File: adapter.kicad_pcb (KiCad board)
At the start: 2 copper layers, 15 parts, among them P1 CONN_02X05, P3 CONN_02X06, Q1 BSS138, U1 MC34063

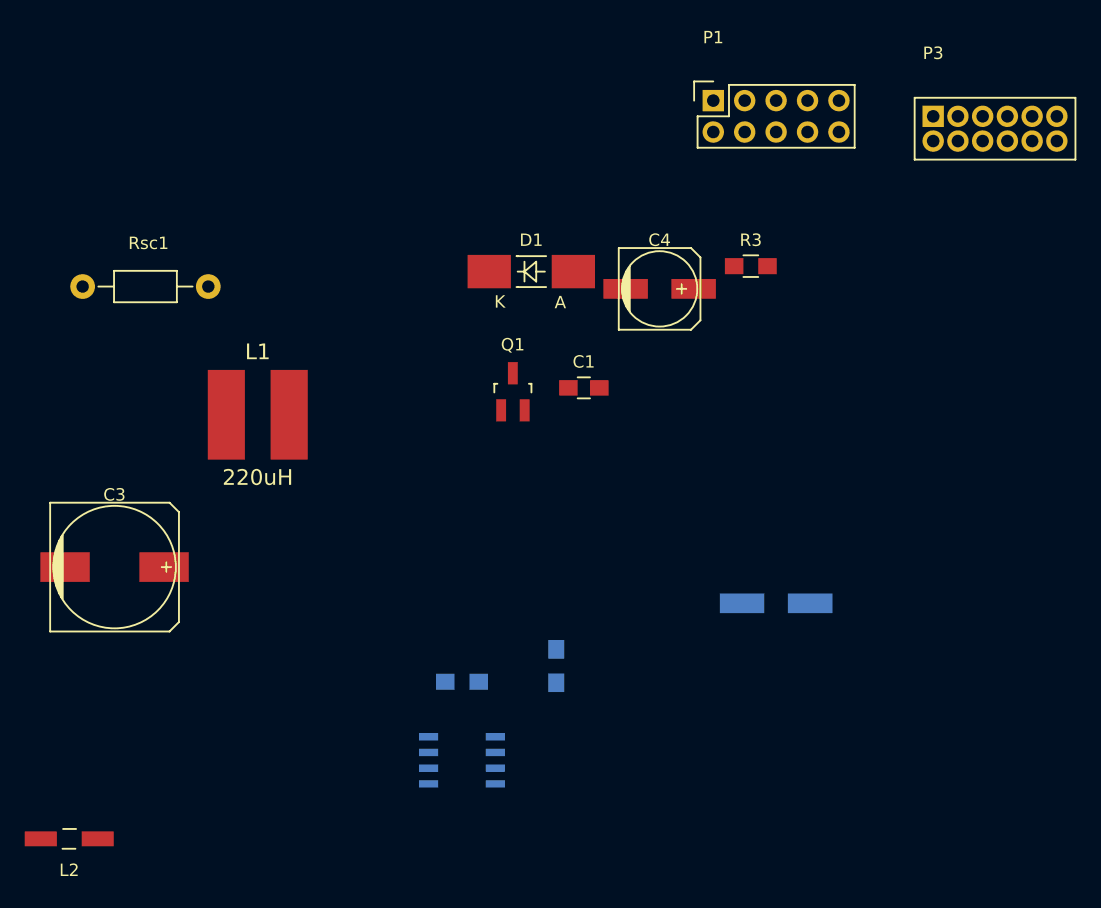
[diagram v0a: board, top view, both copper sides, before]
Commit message: Changed 2mm pitch array footpring a little.
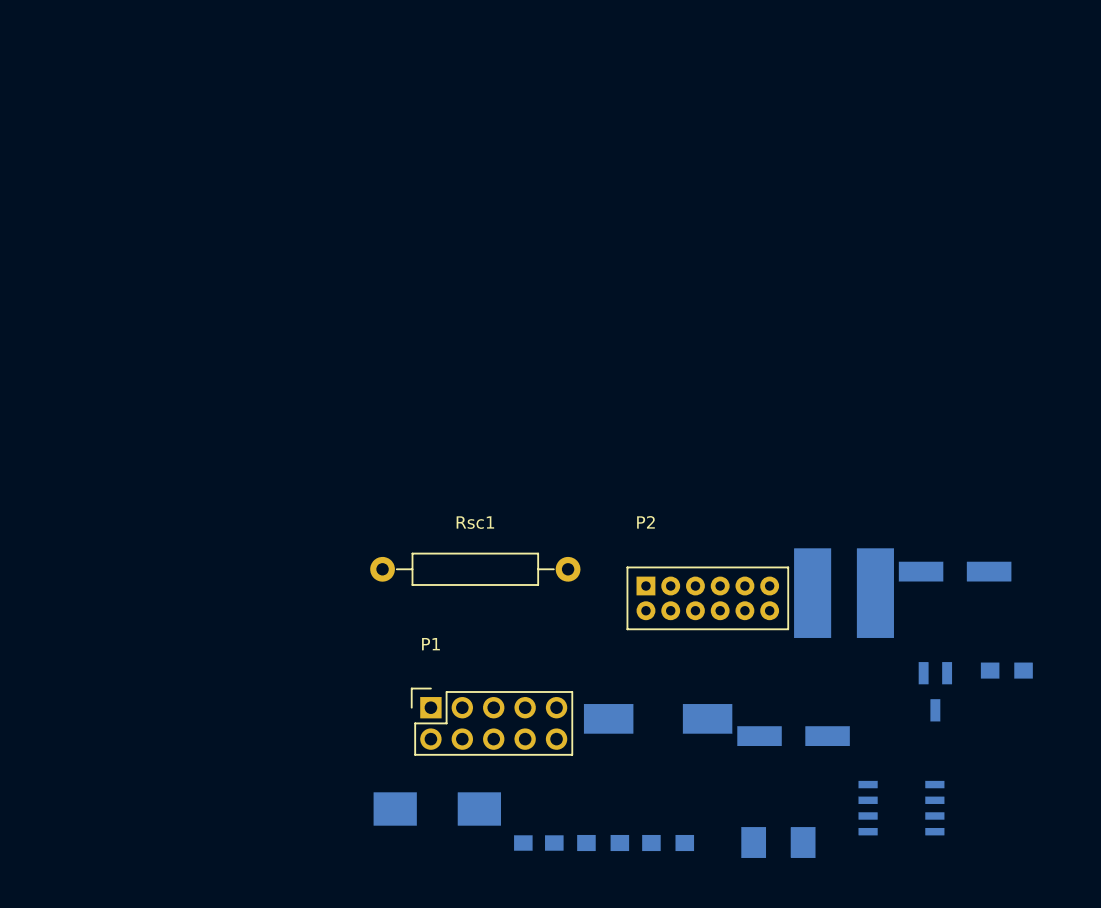
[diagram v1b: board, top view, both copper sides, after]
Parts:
- removed P3: CONN_02X06, DSMX Tx module adapter:Socket_Strip_Straight_2x06_pitch2mm
- added P2: CONN_02X06, DSMX Tx module adapter:Socket_Strip_Straight_2x06_pitch2mm, F.Cu at (181.2, 101.5)
- C1, C3, D1, L1, Q1, R3: moved to B.Cu
- C4: footprint Capacitors_SMD:c_elec_6.3x5.7 -> Capacitors_SMD:c_elec_6.3x7.7; moved to B.Cu
- L2: footprint Choke_SMD:Choke_SMD_1206_Handsoldering -> Capacitors_SMD:C_1210_HandSoldering; moved to B.Cu
- Rsc1: footprint Resistors_ThroughHole:Resistor_Horizontal_RM10mm -> Resistors_ThroughHole:Resistor_Horizontal_RM15mm
- moved L2 57.3 mm to (192.0, 122.2), turned to 0 degrees
- moved P1 54.1 mm to (163.9, 111.3)
- moved L1 49.5 mm to (197.3, 102.1)
- moved C3 45.6 mm to (182.2, 112.2)
- moved D1 44.1 mm to (164.4, 119.5)
- moved Q1 41.9 mm to (204.6, 110.0)
- moved R3 38.7 mm to (210.4, 108.3)
- moved C1 37.0 mm to (172.6, 122.3)
- moved U1 35.7 mm to (201.9, 119.4)
- moved Rsc1 35.1 mm to (167.4, 100.1)
- moved C4 33.1 mm to (206.2, 100.3)
- moved R1 17.3 mm to (177.8, 122.3), turned to 0 degrees
- moved R2 16.9 mm to (183.0, 122.3), turned to 0 degrees
- moved C2 10.8 mm to (193.2, 113.6)
